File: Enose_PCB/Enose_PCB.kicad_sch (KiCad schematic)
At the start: 31 parts, among them J1 Conn_01x04_Pin, J10 Fan, J2 Conn_01x04_Pin, J3 Conn_01x04_Pin, J4 DA15_Pins, Q6 NMOS, SW1 SW_DPST_x2, SW2 SW_DPST_x2, U1 ESP32-S3-WROOM-1

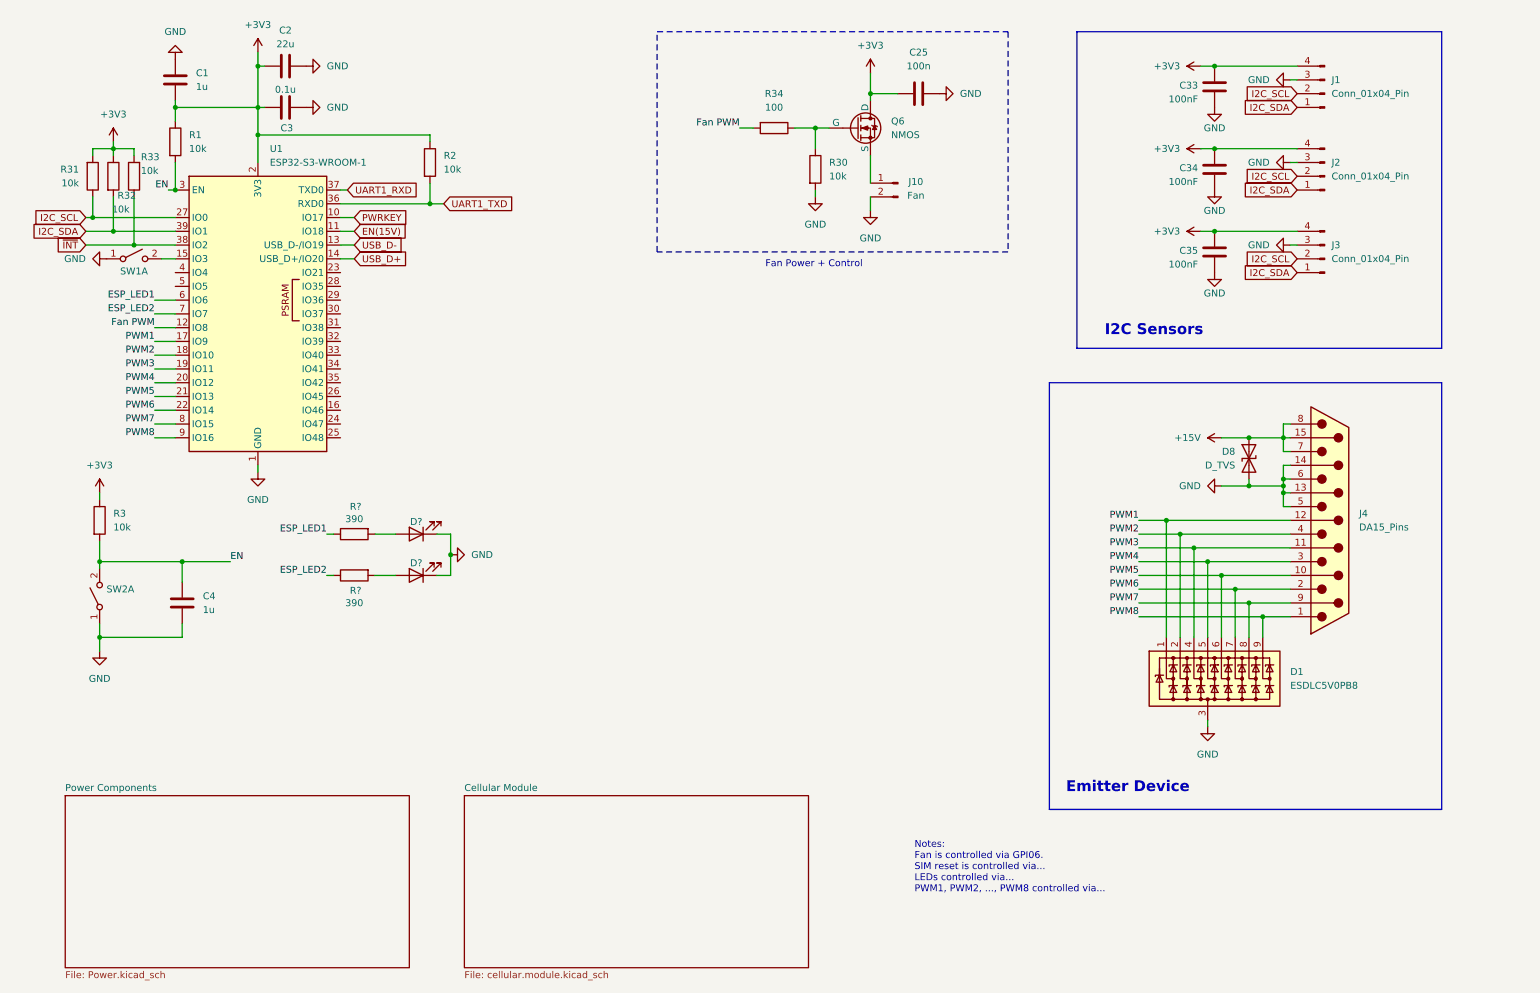
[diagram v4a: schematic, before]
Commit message: Changed Battery Charger
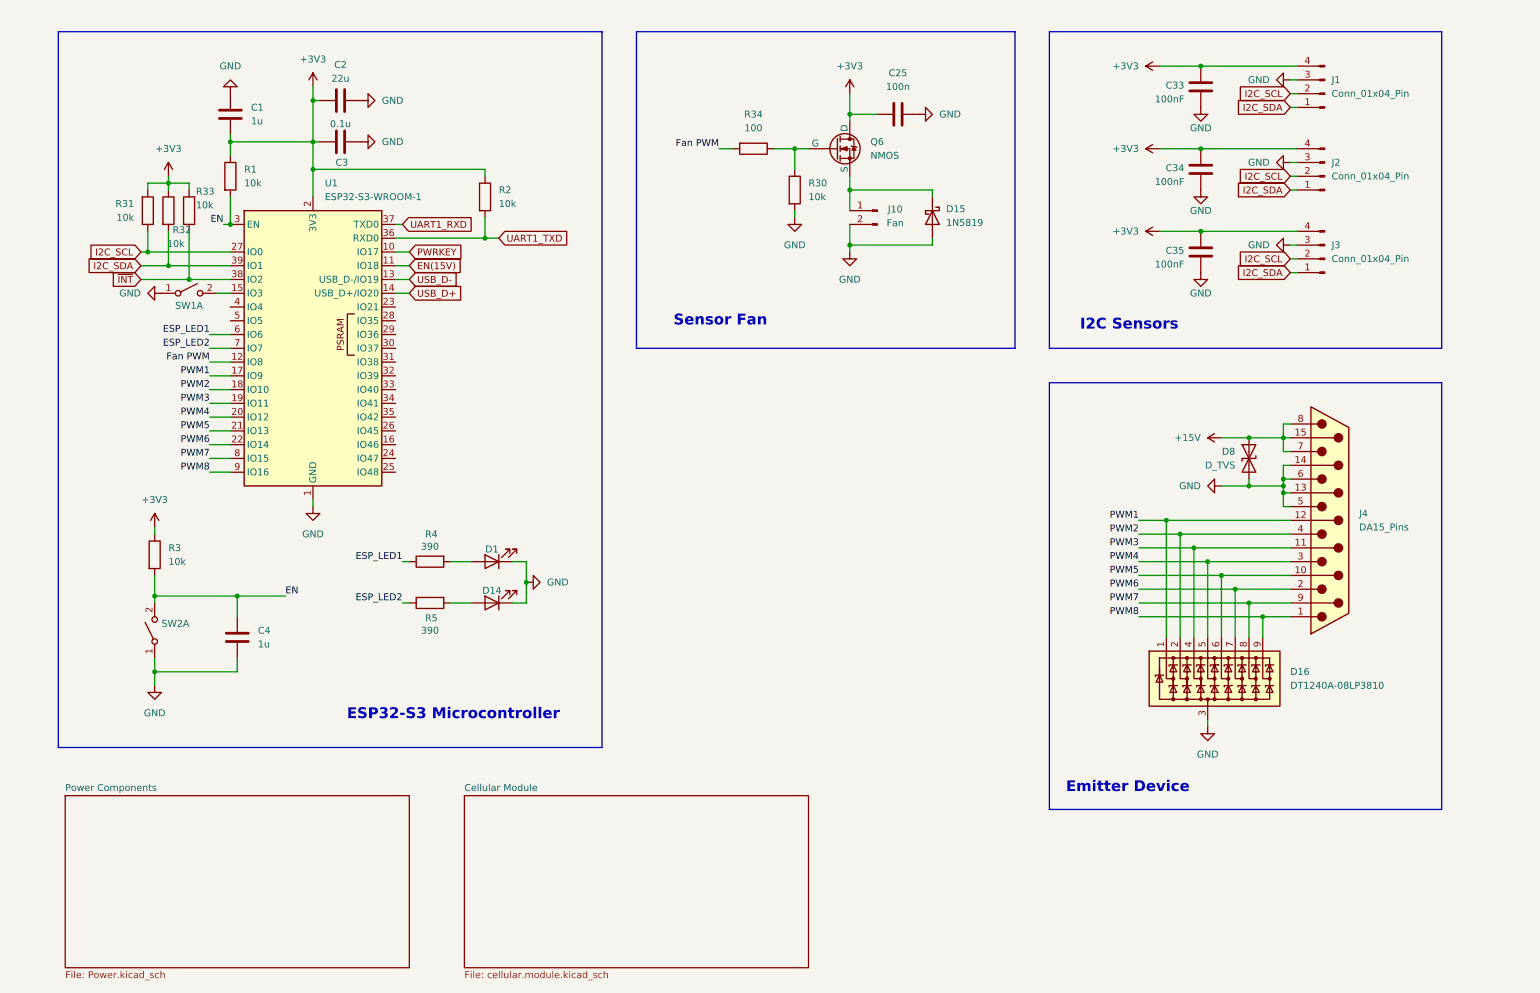
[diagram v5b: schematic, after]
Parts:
- removed D1: ESDLC5V0PB8, Package_DFN_QFN:UDFN-9_1.0x3.8mm_P0.5mm, symbol Power_Protection:ESDLC5V0PB8
- added D15: 1N5819, Diode_THT:D_DO-41_SOD81_P10.16mm_Horizontal, symbol Diode:1N5819
- added D16: DT1240A-08LP3810, Package_DFN_QFN:UDFN-9_1.0x3.8mm_P0.5mm, symbol Power_Protection:DT1240A-08LP3810
- gave numbers to parts that had none: 4
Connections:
- net GND: now also D15.2 (A), D16.3 (A)
- net PWM1: now also D16.1 (K1)
- net PWM2: now also D16.2 (K2)
- net PWM3: now also D16.4 (K3)
- net PWM4: now also D16.5 (K4)
- net PWM5: now also D16.6 (K5)
- net PWM6: now also D16.7 (K6)
- net PWM7: now also D16.8 (K7)
- net PWM8: now also D16.9 (K8)
- net at J10.1 (Pin_1), Q6.3 (S): now also D15.1 (K)
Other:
- note added: "ESP32-S3 Microcontroller"
- note added: "Sensor Fan"
- note removed: "Fan Power + Control"
- note removed: "Notes: Fan is controlled via GPI06. SIM reset is controlled via... LEDs controlled via... PWM1, PWM2, ..., PWM8 controlled via..."
- moved on the sheet: C1, C2, C25, C3, C33, C34, C35, C4, D1, D14, J10, Q6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

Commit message: Added load switch and stuff
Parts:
- removed SW1, SW2: SW_DPST_x2, symbol Switch:SW_DPST_x2
- added C38: 1uF, symbol Device:C
- added C39: 1500pF, symbol Device:C
- added C40: 100nF, symbol Device:C
- added IC3: TPS22958DGNR, SOP65P490X110-9N, symbol SamacSys_Parts:TPS22958DGNR
- added R35, R36, R37, R38, R39, R40, R41, R42: 100, Resistor_SMD:R_0805_2012Metric_Pad1.20x1.40mm_HandSolder, symbol Device:R
- added R43: 100k, symbol Device:R
- added SW1, SW2: SW_SPST, SamacSys_Parts:430181038816, symbol Switch:SW_SPST
- added SW4: SW_SPDT, SamacSys_Parts:OS102011MA1QN1, symbol Switch:SW_SPDT
- C1, C2, C3, C33, C34, C35, C4: footprint (none) -> Capacitor_SMD:C_0805_2012Metric_Pad1.18x1.45mm_HandSolder
- C25: value 100n -> 100nF; footprint (none) -> Capacitor_SMD:C_0805_2012Metric_Pad1.18x1.45mm_HandSolder
- D1, D14: footprint (none) -> LED_SMD:LED_0805_2012Metric_Pad1.15x1.40mm_HandSolder
- D15: footprint Diode_THT:D_DO-41_SOD81_P10.16mm_Horizontal -> Diode_SMD:D_SOD-123
- Q6: footprint Ventsi_Lib:Ventsi_SOT23 -> Package_TO_SOT_SMD:SOT-23-3
- R1, R2, R3, R31, R32, R33, R34, R4, R5: footprint (none) -> Resistor_SMD:R_0805_2012Metric_Pad1.20x1.40mm_HandSolder
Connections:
- net EN: now also SW1.4 (B)
- net GND: now also C38.1, C39.2, C40.1, IC3.6 (GND), IC3.9 (EP), SW1.1 (A), SW2.1 (A), SW4.2 (B)
- net PWM1: now also R35.1; no longer D16.1 (K1), J4.12 (P12)
- net PWM2: now also R36.1; no longer D16.2 (K2), J4.4
- net PWM3: now also R37.1; no longer D16.4 (K3), J4.11 (P111)
- net PWM4: now also R38.1; no longer D16.5 (K4), J4.3
- net PWM5: now also R39.1; no longer D16.6 (K5), J4.10 (P10)
- net PWM6: now also R40.1; no longer D16.7 (K6), J4.2
- net PWM7: now also R41.1; no longer D16.8 (K7), J4.9 (P9)
- net PWM8: now also R42.1; no longer D16.9 (K8), J4.1
- net at U1.15 (IO3): now also SW2.4 (B)
- new net: IC3.2 (ON), R43.1, SW4.1 (A)
- new net: D16.6 (K5), J4.3, R38.2
- new net: D16.4 (K3), J4.2, R40.2
- new net: D16.7 (K6), J4.11 (P111), R37.2
- new net: D16.2 (K2), J4.9 (P9), R41.2
- new net: D16.1 (K1), J4.1, R42.2
- new net: D16.5 (K4), J4.10 (P10), R39.2
- new net: D16.9 (K8), J4.12 (P12), R35.2
- new net: D16.8 (K7), J4.4, R36.2
- new net: C39.1, IC3.7 (CT)
- new net +BATT: C40.2, IC3.5 (VOUT_1), IC3.8 (VOUT_2)
- new net +SYS: C38.2, IC3.1 (VIN_1), IC3.3 (VBIAS), IC3.4 (VIN_2), R43.2
- no-connect marks 0 -> 16
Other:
- note added: "Load Switch"
- note added: "Note: - A load switch is used to accommodate the peak system current during operation (6A), while also limiting the inrush current to safe levels (<2,A). - The Switch is placed on the system/battter rail to allow for battery charging while the system is turned off"

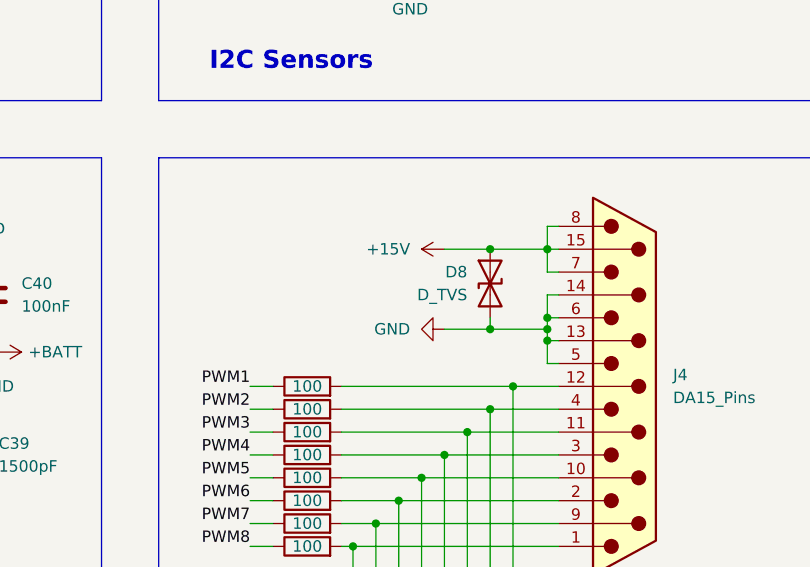
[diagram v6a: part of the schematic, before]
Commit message: Assigned footprints
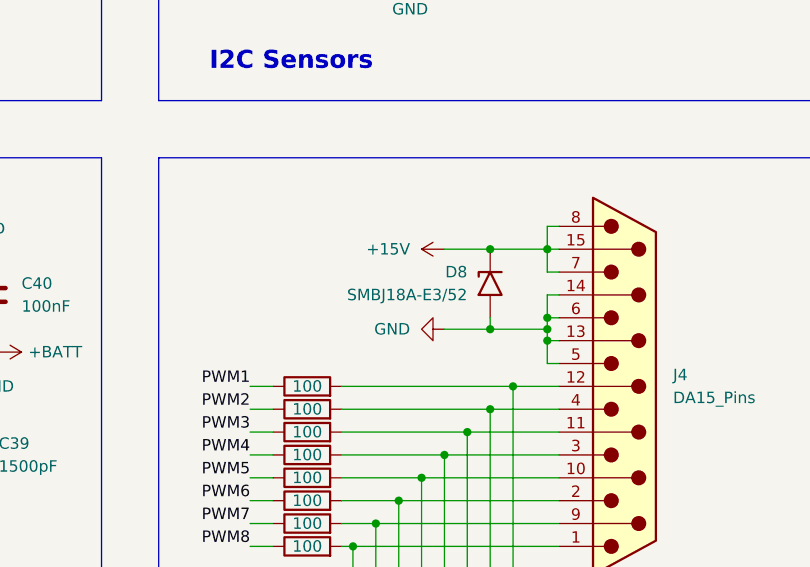
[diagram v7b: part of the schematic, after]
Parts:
- removed D8: D_TVS, symbol Device:D_TVS
- added D8: SMBJ18A-E3/52, Diode_SMD:D_SMB, symbol Diode:SM6T18A
- C38, C39, C40: footprint (none) -> Capacitor_SMD:C_0805_2012Metric_Pad1.18x1.45mm_HandSolder
- IC3: footprint SOP65P490X110-9N -> SamacSys_Parts:SOP65P490X110-9N
- J1: footprint (none) -> Connector_PinHeader_2.54mm:PinHeader_1x04_P2.54mm_Vertical
- J10: footprint Connector_PinHeader_2.54mm:PinHeader_1x02_P2.54mm_Vertical -> Connector_JST:JST_XH_B2B-XH-AM_1x02_P2.50mm_Vertical
- J2, J3: footprint (none) -> Connector_JST:JST_XH_B4B-XH-A_1x04_P2.50mm_Vertical
- J4: footprint (none) -> Connector_Dsub:DSUB-15_Pins_Horizontal_P2.77x2.84mm_EdgePinOffset9.40mm
- R43: footprint (none) -> Resistor_SMD:R_0805_2012Metric_Pad1.20x1.40mm_HandSolder
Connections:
- net +15V: now also D8.1 (A1)
- net GND: now also D8.2 (A2)
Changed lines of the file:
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@@
 	)
 	(junction
-		(at 240.03 92.71)
-		(diameter 0)
-		(color 0 0 0 0)
-	)
-	(junction
 		(at 140.97 104.14)
 		(diameter 0)
@@
 	)
 	(junction
+		(at 240.03 92.71)
+		(diameter 0)
+		(color 0 0 0 0)
+	)
+	(junction
 		(at 67.31 43.18)
 		(diameter 0)
@@
 	(wire
 		(pts
-			(xy 240.03 92.71) (xy 246.38 92.71)
+			(xy 234.95 92.71) (xy 240.03 92.71)
 		)
 		(stroke
@@
 	(wire
 		(pts
-			(xy 48.26 99.06) (xy 52.07 99.06)
+			(xy 240.03 92.71) (xy 246.38 92.71)
 		)
 		(stroke
@@
 	(wire
 		(pts
-			(xy 44.45 45.72) (xy 40.64 45.72)
+			(xy 48.26 99.06) (xy 52.07 99.06)
 		)
 		(stroke
@@
 	(wire
 		(pts
-			(xy 181.61 46.99) (xy 166.37 46.99)
+			(xy 44.45 45.72) (xy 40.64 45.72)
 		)
 		(stroke
@@
 	(wire
 		(pts
-			(xy 184.15 104.14) (xy 185.42 104.14)
+			(xy 181.61 46.99) (xy 166.37 46.99)
 		)
 		(stroke
@@
 	(wire
 		(pts
-			(xy 234.95 92.71) (xy 240.03 92.71)
+			(xy 184.15 104.14) (xy 185.42 104.14)
 		)
 		(stroke
@@
 			)
 		)
-		(property "Footprint" ""
+		(property "Footprint" "Resistor_SMD:R_0805_2012Metric_Pad1.20x1.40mm_HandSolder"
 			(at 139.192 107.95 90)
 			(effects
@@
 			)
 		)
-		(property "Footprint" ""
+		(property "Footprint" "Connector_Dsub:DSUB-15_Pins_Horizontal_P2.77x2.84mm_EdgePinOffset9.40mm"
 			(at 255.27 107.95 0)
 			(effects
@@
 			)
 		)
-		(property "Footprint" ""
+		(property "Footprint" "Capacitor_SMD:C_0805_2012Metric_Pad1.18x1.45mm_HandSolder"
 			(at 182.5752 119.38 0)
 			(effects
@@
 			)
 		)
-		(property "Footprint" ""
+		(property "Footprint" "Connector_JST:JST_XH_B4B-XH-A_1x04_P2.50mm_Vertical"
 			(at 254 59.69 0)
 			(effects
@@
 			)
 		)
-		(property "Footprint" ""
+		(property "Footprint" "Connector_PinHeader_2.54mm:PinHeader_1x04_P2.54mm_Vertical"
 			(at 254 29.21 0)
 			(effects
@@
 			)
 		)
-		(property "Footprint" ""
+		(property "Footprint" "Capacitor_SMD:C_0805_2012Metric_Pad1.18x1.45mm_HandSolder"
 			(at 140.0048 101.6 0)
 			(effects
@@
 	)
 	(symbol
+		(lib_id "Diode:SM6T18A")
+		(at 240.03 96.52 90)
+		(mirror x)
+		(unit 1)
+		(exclude_from_sim no)
+		(in_bom yes)
+		(on_board yes)
+		(dnp no)
+		(property "Reference" "D8"
+			(at 237.49 95.2499 90)
+			(effects
+				(font
+					(size 1.27 1.27)
+				)
+				(justify left)
+			)
+		)
+		(property "Value" "SMBJ18A-E3/52"
+			(at 237.49 97.7899 90)
+			(effects
+				(font
+					(size 1.27 1.27)
+				)
+				(justify left)
+			)
+		)
+		(property "Footprint" "Diode_SMD:D_SMB"
+			(at 245.11 96.52 0)
+			(effects
+				(font
+					(size 1.27 1.27)
+				)
+				(hide yes)
+			)
+		)
+		(property "Datasheet" "http://www.vishay.com/docs/88392/smbj.pdf"
+			(at 240.03 95.25 0)
+			(effects
+				(font
+					(size 1.27 1.27)
+				)
+				(hide yes)
+			)
+		)
+		(property "Description" "Vishay SMBJ18A-E3/52, Uni-Directional TVS Diode, 600W, 2-Pin DO-214AA"
+			(at 240.03 96.52 0)
+			(effects
+				(font
+					(size 1.27 1.27)
+				)
+				(hide yes)
+			)
+		)
+		(pin "2"
+		)
+		(pin "1"
+		)
+		(instances
+			(project ""
+				(path "/eef70be0-4107-491c-8ca0-465071a6397e"
+					(reference "D8")
+					(unit 1)
+				)
+			)
+		)
+	)
+	(symbol
 		(lib_id "power:+BATT")
 		(at 138.43 104.14 90)
@@
 			)
 		)
-		(property "Footprint" ""
+		(property "Footprint" "Capacitor_SMD:C_0805_2012Metric_Pad1.18x1.45mm_HandSolder"
 			(at 185.1152 101.6 0)
 			(effects
@@
 			)
 		)
-		(property "Footprint" ""
+		(property "Footprint" "Connector_JST:JST_XH_B4B-XH-A_1x04_P2.50mm_Vertical"
 			(at 254 44.45 0)
 			(effects
@@
 	)
 	(symbol
-		(lib_id "Device:D_TVS")
-		(at 240.03 96.52 90)
-		(mirror x)
-		(unit 1)
-		(exclude_from_sim no)
-		(in_bom yes)
-		(on_board yes)
-		(dnp no)
-		(property "Reference" "D8"
-			(at 237.49 95.2499 90)
-			(effects
-				(font
-					(size 1.27 1.27)
-				)
-				(justify left)
-			)
-		)
-		(property "Value" "D_TVS"
-			(at 237.49 97.7899 90)
-			(effects
-				(font
-					(size 1.27 1.27)
-				)
-				(justify left)
-			)
-		)
-		(property "Footprint" ""
-			(at 240.03 96.52 0)
-			(effects
-				(font
-					(size 1.27 1.27)
-				)
-				(hide yes)
-			)
-		)
-		(property "Datasheet" "~"
-			(at 240.03 96.52 0)
-			(effects
-				(font
-					(size 1.27 1.27)
-				)
-				(hide yes)
-			)
-		)
-		(property "Description" "Bidirectional transient-voltage-suppression diode"
-			(at 240.03 96.52 0)
-			(effects
-				(font
-					(size 1.27 1.27)
-				)
-				(hide yes)
-			)
-		)
-		(pin "1"
-		)
-		(pin "2"
-		)
-		(instances
-			(project ""
-				(path "/eef70be0-4107-491c-8ca0-465071a6397e"
-					(reference "D8")
-					(unit 1)
-				)
-			)
-		)
-	)
-	(symbol
 		(lib_id "power:GND")
 		(at 156.21 52.07 0)
@@
 			)
 		)
-		(property "Footprint" "SOP65P490X110-9N"
+		(property "Footprint" "SamacSys_Parts:SOP65P490X110-9N"
 			(at 176.53 196.52 0)
 			(effects
@@
 			)
 		)
-		(property "Footprint" "Connector_PinHeader_2.54mm:PinHeader_1x02_P2.54mm_Vertical"
+		(property "Footprint" "Connector_JST:JST_XH_B2B-XH-AM_1x02_P2.50mm_Vertical"
 			(at 171.45 50.8 0)
 			(effects
